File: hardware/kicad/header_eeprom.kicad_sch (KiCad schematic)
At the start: 0 parts

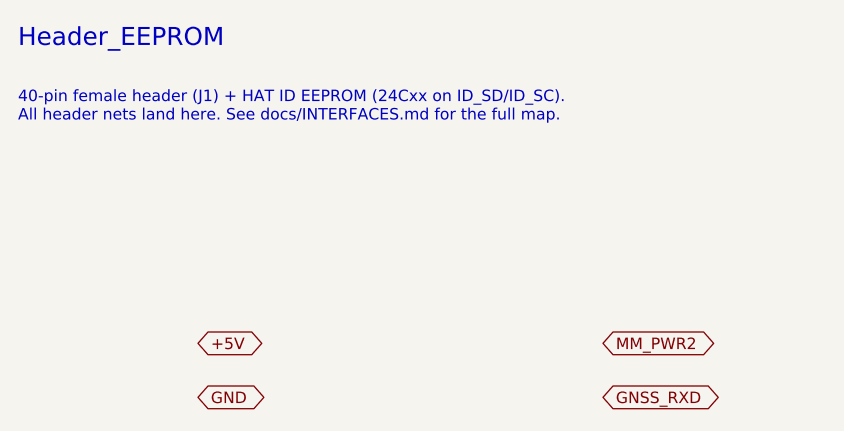
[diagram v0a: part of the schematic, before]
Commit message: Deepen design to component level + fix EEPROM power rail
- Fix: HAT ID EEPROM (U6) now powered from Pi header 3V3 (3V3_PI, pin 1)
  so it is readable at boot before the HAT's own 3V3 comes up (was
  incorrectly on the HAT 3V3 regulator).
- Add docs/SCHEMATIC.md: component-level subcircuits for every block
  (refdes + values + nets) — buck-boost/3V3 FB dividers, MM8108 SPI
  termination/pulls, E21 RF DC-blocks/attenuator pad/T-R pulldowns,
  NEO-M9N active-antenna bias via VCC_RF, ID EEPROM (WP default).
- Add docs/BRINGUP.md: stage-gated power-on + RF test plan (don't key
  the 1W PA until rails/drive-level/FEM-timing verified).
- Add GNSS VCC_RF antenna bias + +3V3_GNSS ferrite to the net list.
- Enrich KiCad sub-sheets with per-block refdes notes and the new nets;
  regenerate scaffold (KiCad 10 format, S-expression balance re-checked).
- BOM: concrete passives (RF DC-blocks, attenuator pad, ferrite, TVS,
  FB dividers, WP jumper).

https://claude.ai/code/session_015nkkW85U3sPf5mcvrsMw7T
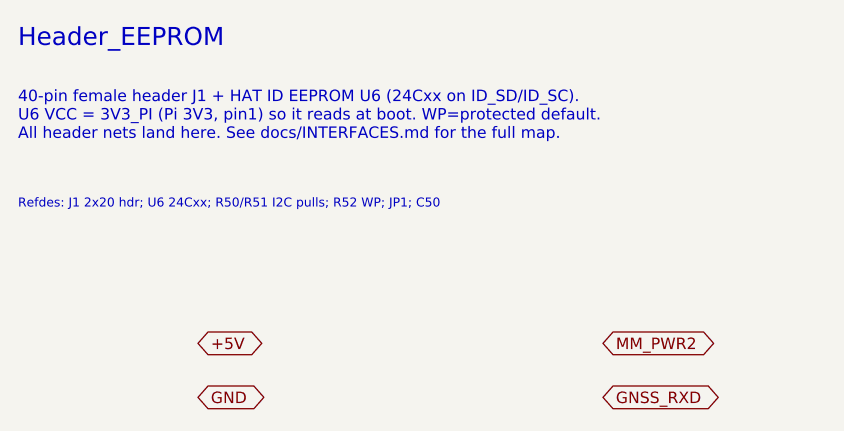
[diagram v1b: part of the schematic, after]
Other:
- note added: "40-pin female header J1 + HAT ID EEPROM U6 (24Cxx on ID_SD/ID_SC). U6 VCC = 3V3_PI (Pi 3V3, pin1) so it reads at boot. WP=protected default. All header nets land here. See docs/INTERFACES.md for the full map."
- note added: "Refdes: J1 2x20 hdr; U6 24Cxx; R50/R51 I2C pulls; R52 WP; JP1; C50"
- note removed: "40-pin female header (J1) + HAT ID EEPROM (24Cxx on ID_SD/ID_SC). All header nets land here. See docs/INTERFACES.md for the full map."
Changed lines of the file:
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@@
 	(paper "A4")
 	(text "Header_EEPROM" (exclude_from_sim no) (at 20 15 0) (effects (font (size 2 2) (thickness 0.3)) (justify left top)))
-	(text "40-pin female header (J1) + HAT ID EEPROM (24Cxx on ID_SD/ID_SC).\nAll header nets land here. See docs/INTERFACES.md for the full map." (exclude_from_sim no) (at 20 22 0) (effects (font (size 1.27 1.27)) (justify left top)))
+	(text "40-pin female header J1 + HAT ID EEPROM U6 (24Cxx on ID_SD/ID_SC).\nU6 VCC = 3V3_PI (Pi 3V3, pin1) so it reads at boot. WP=protected default.\nAll header nets land here. See docs/INTERFACES.md for the full map." (exclude_from_sim no) (at 20 22 0) (effects (font (size 1.27 1.27)) (justify left top)))
+	(text "Refdes: J1 2x20 hdr; U6 24Cxx; R50/R51 I2C pulls; R52 WP; JP1; C50" (exclude_from_sim no) (at 20 34 0) (effects (font (size 1.0 1.0)) (justify left top)))
 	(global_label "+5V" (shape bidirectional) (at 40 50 0) (fields_autoplaced yes) (effects (font (size 1.27 1.27)) (justify left)))
 	(global_label "GND" (shape bidirectional) (at 40 56 0) (fields_autoplaced yes) (effects (font (size 1.27 1.27)) (justify left)))

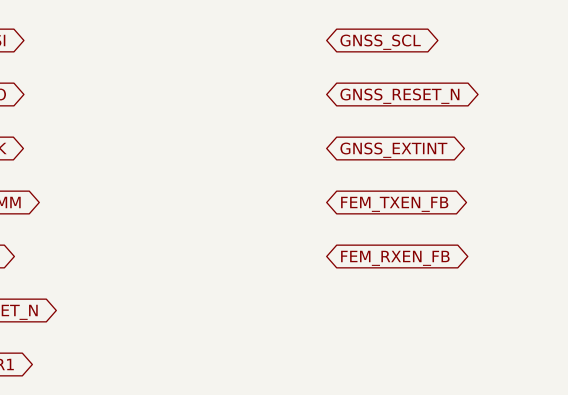
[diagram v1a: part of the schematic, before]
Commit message: Add gap-analysis components (datasheet-grounded) + RTC
Read the uploaded datasheets (MM8108-MF15457, E21-900G30S, NEO-M9N-00B)
and resolved the component gaps:

- #1/#2 RESOLVED by the module: MF15457 is self-contained (internal
  clock+PMU+PA); only needs VBAT/VBAT_TX/VDDIO 3.0-3.6 V. No external SoC
  inductors, 1V8/1V2 rails, or TCXO.
- VPA fixed at 5.0 V (E21 needs 4.75-5.25 V, ~620 mA TX, +20 dBm in ->
  +30 dBm out, 12 dB gain). Real pinouts wired (module 38-pin; E21
  pin6=PIN xcvr, pin9=ANT).
- Architecture finding: module has integrated PA + single ANT pin and NO
  hardware T/R FEM line. External E21 now needs (a) ~3-5 dB drive pad,
  (b) T/R control via module GPIO0/1 toggled by OpenMANET FW (or RF-sense
  auto-T/R fallback), and (c) end-product recertification at +30 dBm.

Added components:
- N3 900 MHz harmonic LPF (FL2); N4 inrush soft-start load switch (U10);
  N5 supervisor (U11); N6 radio-rail load switch (U12, OpenMANET
  power-gpios); N7 RF shields; N8 GNSS antenna ESD (D8); N9 status LEDs;
  N10 E21 thermal relief.
- RTC: RV-3028-C7 (U13) on I2C1 0x52 with a soldered rechargeable cell
  (BT1, trickle-charged) per request; added to the device-tree overlay.
- Declined per request: debug UART/JTAG pads, test points.

Updated docs (new COMPONENTS_GAP.md; DECISIONS B1-B9; SCHEMATIC; BOM;
POWER budget), netlist, overlay, and regenerated the KiCad 10 scaffold
with the new nets. Committed the vendor datasheets under hardware/.

https://claude.ai/code/session_015nkkW85U3sPf5mcvrsMw7T
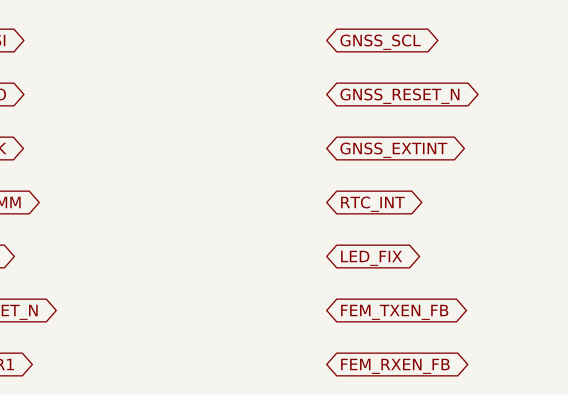
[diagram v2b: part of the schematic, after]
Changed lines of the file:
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@@
 	(global_label "GNSS_RESET_N" (shape bidirectional) (at 85 86 0) (fields_autoplaced yes) (effects (font (size 1.27 1.27)) (justify left)))
 	(global_label "GNSS_EXTINT" (shape bidirectional) (at 85 92 0) (fields_autoplaced yes) (effects (font (size 1.27 1.27)) (justify left)))
-	(global_label "FEM_TXEN_FB" (shape bidirectional) (at 85 98 0) (fields_autoplaced yes) (effects (font (size 1.27 1.27)) (justify left)))
-	(global_label "FEM_RXEN_FB" (shape bidirectional) (at 85 104 0) (fields_autoplaced yes) (effects (font (size 1.27 1.27)) (justify left)))
+	(global_label "RTC_INT" (shape bidirectional) (at 85 98 0) (fields_autoplaced yes) (effects (font (size 1.27 1.27)) (justify left)))
+	(global_label "LED_FIX" (shape bidirectional) (at 85 104 0) (fields_autoplaced yes) (effects (font (size 1.27 1.27)) (justify left)))
+	(global_label "FEM_TXEN_FB" (shape bidirectional) (at 85 110 0) (fields_autoplaced yes) (effects (font (size 1.27 1.27)) (justify left)))
+	(global_label "FEM_RXEN_FB" (shape bidirectional) (at 85 116 0) (fields_autoplaced yes) (effects (font (size 1.27 1.27)) (justify left)))
 )

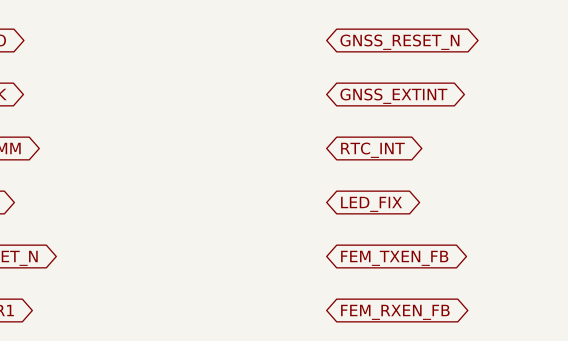
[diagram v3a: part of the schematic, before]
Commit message: Pivot to MM8108-M20 primary / MF15457 fallback; retire external E21
Per the decision to make the MM8108-M20 the primary radio (with MF15457
as the build-today fallback) and retire the external E21 PA path:

Design:
- One radio site fed by the shared SPI/control nets accepts either module.
- Removed the E21 PA, 5V buck-boost (VPA), harmonic LPF, drive pad, T/R
  control, RF-sense VOX, and RF bypass. Both modules drive the antenna
  directly (M20 = integrated 28.5 dBm PA + 902-928 SAW, certified;
  MF15457 = ~27 dBm). Power collapses to a single 3V3 rail.
- Header GPIO4/6 (old FEM fallback) revert to spares; GPIO12/13 drive the
  status LEDs.
- M20 pinout/power/footprint held at placeholder pending its datasheet
  (B12); MF15457 pin-level detail stays the concrete baseline.

Docs updated: DECISIONS (A3 superseded, B11/B12 added, B2-B5/B10 retired,
new radio-options table + order), DESIGN, SCHEMATIC, POWER, RF, BOM,
INTERFACES, COMPONENTS_GAP, LINK_BUDGET, FIRMWARE_PA, BRINGUP, MECHANICAL,
README. Netlist, KiCad scaffold (sheets/silk/root note), and the OpenMANET
overlay/README updated to match. Scaffold regenerated and validated.

https://claude.ai/code/session_015nkkW85U3sPf5mcvrsMw7T
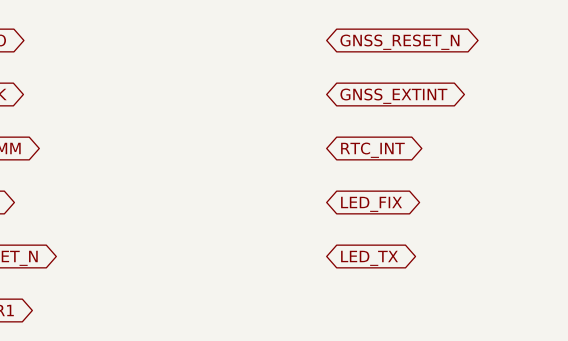
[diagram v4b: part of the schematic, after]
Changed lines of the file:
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@@
 	(global_label "RTC_INT" (shape bidirectional) (at 85 98 0) (fields_autoplaced yes) (effects (font (size 1.27 1.27)) (justify left)))
 	(global_label "LED_FIX" (shape bidirectional) (at 85 104 0) (fields_autoplaced yes) (effects (font (size 1.27 1.27)) (justify left)))
-	(global_label "FEM_TXEN_FB" (shape bidirectional) (at 85 110 0) (fields_autoplaced yes) (effects (font (size 1.27 1.27)) (justify left)))
-	(global_label "FEM_RXEN_FB" (shape bidirectional) (at 85 116 0) (fields_autoplaced yes) (effects (font (size 1.27 1.27)) (justify left)))
+	(global_label "LED_TX" (shape bidirectional) (at 85 110 0) (fields_autoplaced yes) (effects (font (size 1.27 1.27)) (justify left)))
 )
